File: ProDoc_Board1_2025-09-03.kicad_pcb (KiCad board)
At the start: 2 copper layers, 60 x 45.5 mm, 13 parts, among them CN10 A2502-WV02, CN11 A2502-WV02, CN2 B04B-XNISK-A-1(LF)(SN), CN3 B04B-XNISK-A-1(LF)(SN), CN4 B04B-XNISK-A-1(LF)(SN), CN7 XH2.54-5PIN, CN8 A2502-WV02, CN9 A2502-WV02, J1 Conn_01x05_Pin, U3 Ra-02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

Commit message: schenatic done
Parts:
- added C1: C_STAT, Capacitor_SMD:C_1210_3225Metric, B.Cu at (109.6, 53.1)
- added C2: C_PVL, Capacitor_SMD:C_0402_1005Metric, B.Cu at (98.5, 52.0)
- added C3: C_AVL, Capacitor_SMD:C_0402_1005Metric, B.Cu at (98.5, 50.0)
- added C4: C_BST2, Capacitor_SMD:C_0402_1005Metric, B.Cu at (98.5, 48.0)
- added C5: C_BST1, Capacitor_SMD:C_0402_1005Metric, B.Cu at (98.5, 46.1)
- added C6: C_BATT, Capacitor_SMD:C_0805_2012Metric, B.Cu at (103.0, 45.2)
- added C7: C_OUT1, Capacitor_SMD:C_1210_3225Metric_Pad1.33x2.70mm_HandSolder, B.Cu at (103.8, 53.1)
- added C8: C_OUT2, Capacitor_SMD:C_1210_3225Metric_Pad1.33x2.70mm_HandSolder, B.Cu at (103.8, 48.8)
- added C9: C_CHGIN, Capacitor_SMD:C_1210_3225Metric, B.Cu at (109.6, 48.8)
- added D1: LED, Diode_SMD:D_01005_0402Metric, B.Cu at (98.4, 44.3)
- added D3: D_Schottky_Small, Diode_SMD:D_SOD-323, B.Cu at (109.2, 60.0)
- added J2: Conn_01x02_Pin, Connector_JST:JST_SH_BM02B-SRSS-TB_1x02-1MP_P1.00mm_Vertical, B.Cu at (104.2, 64.6)
- added L1: L, ProDoc_Board1_2025-09-03:CMLE063T-2R2MS, B.Cu at (88.6, 52.2)
- added R1: R_OTGEN, Resistor_SMD:R_0805_2012Metric, B.Cu at (89.7, 66.2)
- added R10: R_ITO, Resistor_SMD:R_0805_2012Metric, B.Cu at (94.1, 54.4)
- added R11: R_VSET, Resistor_SMD:R_0805_2012Metric, B.Cu at (98.5, 66.2)
- added R12: R_INTB, Resistor_SMD:R_0805_2012Metric, B.Cu at (98.5, 63.3)
- added R13: R_SDA, Resistor_SMD:R_0805_2012Metric, B.Cu at (98.5, 60.3)
- added R14: R_SCL, Resistor_SMD:R_0805_2012Metric, B.Cu at (98.5, 57.4)
- added R15: R_SENSE, Resistor_SMD:R_1206_3216Metric, B.Cu at (109.6, 45.0)
- added R2: R_DISQBAT, Resistor_SMD:R_0805_2012Metric, B.Cu at (89.7, 63.3)
- added R3: R_STBY, Resistor_SMD:R_0805_2012Metric, B.Cu at (89.7, 60.3)
- added R4: R_TB, Resistor_SMD:R_0805_2012Metric, B.Cu at (89.7, 57.4)
- added R5: R_ISET, Resistor_SMD:R_0805_2012Metric, B.Cu at (89.7, 54.4)
- added R6: R_INOKB, Resistor_SMD:R_0805_2012Metric, B.Cu at (94.1, 66.2)
- added R7: R_STAT, Resistor_SMD:R_0805_2012Metric, B.Cu at (94.1, 63.3)
- added R8: R_PVL, Resistor_SMD:R_0805_2012Metric, B.Cu at (94.1, 60.3)
- added R9: R_INLIM, Resistor_SMD:R_0805_2012Metric, B.Cu at (94.1, 57.4)
- added U1: MAX77961EFV06+, ProDoc_Board1_2025-09-03:MAX77961, B.Cu at (142.6, 86.0)
- CN10: value A2502-WV02 -> BATT; moved to B.Cu
- CN11: value A2502-WV02 -> CHGIN; moved to B.Cu
- moved CN10 109.6 mm to (71.0, 59.7), turned to 0 degrees
- moved D2 85.3 mm to (78.3, 60.9), turned to 0 degrees
- moved CN11 50.3 mm to (127.5, 84.8), turned to -90 degrees
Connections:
- net Net-(U4-OUT+) renamed PULLUP
- CN10 pad 1: GND -> BATT-
- CN10 pad 2: Net-(CN10-Pad2) -> BATT+
- CN11 pad 1: Net-(CN10-Pad2) -> BATT-
- CN11 pad 2: Net-(D2-A) -> CSINN
- CN2 pad 1: GND -> BATT-
- CN3 pad 1: GND -> BATT-
- CN4 pad 1: GND -> BATT-
- CN7 pad 1: GND -> BATT-
- CN8 pad 1: GND -> BATT-
- CN9 pad 1: GND -> BATT-
- D2 pad 2: Net-(D2-A) -> SYS
- H1 pad 14: GND -> BATT-
- H1 pad 25: GND -> BATT-
- H1 pad 36: unconnected-(H1-Pad36) -> STAT
- H1 pad 39: GND -> BATT-
- H1 pad 9: GND -> BATT-
- J1 pad 4: GND -> BATT-
- J1 pad 5: GND -> BATT-
- U3 pad 16: GND -> BATT-
- U4 pad 2: GND -> BATT-
- U4 pad 4: GND -> BATT-
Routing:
- net Net-(D2-A): track 28.4 -> 0.00 mm, vias 2 -> 0
- net Net-(D2-K): track 25.7 -> 0.95 mm, vias 2 -> 0
- net Net-(CN10-Pad2): track 11.0 -> 0.00 mm
- net GND: vias 1 -> 0
- net BATT-: vias 0 -> 1
- added copper zone on B.Cu, net BATT-
- added copper zone on F.Cu, net BATT-
- removed copper zone on B.Cu, net GND
- removed copper zone on F.Cu, net GND

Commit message: layout started
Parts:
- added C10: C_CSINN, Capacitor_SMD:C_0402_1005Metric, B.Cu at (160.3, 82.6)
- added C11: C_CINP, Capacitor_SMD:C_0402_1005Metric, B.Cu at (161.7, 82.6)
- added C12: C_DIFF, Capacitor_SMD:C_0402_1005Metric, B.Cu at (161.0, 84.2)
- added R16: R_CSINP, Resistor_SMD:R_0402_1005Metric, B.Cu at (162.8, 82.6)
- added R17: R_CINN, Resistor_SMD:R_0402_1005Metric, B.Cu at (159.2, 82.5)
- C7, C8: footprint Capacitor_SMD:C_1210_3225Metric_Pad1.33x2.70mm_HandSolder -> Capacitor_SMD:C_1210_3225Metric
- CN10, CN11: footprint Connector_JST:JST_SH_BM02B-SRSS-TB_1x02-1MP_P1.00mm_Vertical -> Connector_JST:JST_VH_B2P-VH_1x02_P3.96mm_Vertical
- CN9: moved to B.Cu
- moved C7 67.0 mm to (159.0, 91.1), turned to 90 degrees
- moved C8 66.6 mm to (155.2, 91.1), turned to 90 degrees
- moved R15 62.3 mm to (161.0, 80.2), turned to 180 degrees
- moved C9 58.8 mm to (155.2, 86.0), turned to -90 degrees
- moved CN11 48.4 mm to (175.8, 84.2)
- moved CN9 6.23 mm to (126.6, 87.0), turned to 90 degrees
- moved U1 5.82 mm to (148.4, 86.6), turned to 90 degrees
- moved U4 2.47 mm to (156.0, 87.9)
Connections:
- C3 pad 1: Vavl -> PULLUP
- CN11 pad 2: CSINN -> Net-(CN11-Pad2)
- CN9 pad 2: PULLUP -> Net-(U4-OUT+)
- H1 pad 2: PULLUP -> Net-(U4-OUT+)
- R15 pad 1: CSINN -> Net-(CN11-Pad2)
- R4 pad 1: Vavl -> PULLUP
- R8 pad 2: Vavl -> PULLUP
- U1 pad 26: Vavl -> PULLUP
- U1 pad 29: CHGIN -> CSINP
- U4 pad 3: PULLUP -> Net-(U4-OUT+)
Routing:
- net PULLUP: track 13.3 -> 0.00 mm
- net Net-(D2-K): track 0.95 -> 0.00 mm

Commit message: temp
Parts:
- CN10, CN11: footprint Connector_JST:JST_VH_B2P-VH_1x02_P3.96mm_Vertical -> Connector_JST:JST_XH_B2B-XH-A_1x02_P2.50mm_Vertical
- R1, R10, R11, R12, R13, R14, R2, R3, R4, R5, R6, R7, R8, R9: footprint Resistor_SMD:R_0805_2012Metric -> Resistor_SMD:R_0402_1005Metric
- moved CN10 109.4 mm to (175.0, 93.7)
- moved L1 91.2 mm to (171.2, 90.9), turned to 90 degrees
- moved C4 68.3 mm to (151.6, 91.0), turned to 180 degrees
- moved C5 65.6 mm to (152.1, 83.9), turned to 180 degrees
- moved C6 64.6 mm to (148.0, 91.6), turned to 180 degrees
- moved R8 60.6 mm to (150.0, 83.8), turned to 180 degrees
- moved C2 59.7 mm to (150.7, 80.9), turned to 90 degrees
- moved C3 59.5 mm to (149.4, 80.9), turned to 90 degrees
- moved CN11 2.19 mm to (177.4, 85.7), turned to 180 degrees
- moved C7 2.01 mm to (158.8, 89.1)
- moved C8 2.01 mm to (155.0, 89.1)
- moved C9 1.81 mm to (155.0, 84.2)
- moved U1 1.66 mm to (149.9, 87.3)
- moved C10 0.58 mm to (160.0, 83.1)
- moved C11 0.58 mm to (161.4, 83.1)
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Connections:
- C1 pad 2: BATT- -> PGND
- C10 pad 2: BATT- -> PGND
- C11 pad 1: BATT- -> PGND
- C2 pad 2: BATT- -> PGND
- C3 pad 2: BATT- -> PGND
- C6 pad 2: BATT- -> PGND
- C7 pad 2: BATT- -> PGND
- C8 pad 2: BATT- -> PGND
- C9 pad 2: BATT- -> PGND
- CN11 pad 1: BATT- -> PGND
- CN2 pad 1: BATT- -> PGND
- CN3 pad 1: BATT- -> PGND
- CN4 pad 1: BATT- -> PGND
- CN7 pad 1: BATT- -> PGND
- CN8 pad 1: BATT- -> PGND
- CN9 pad 1: BATT- -> PGND
- H1 pad 14: BATT- -> PGND
- H1 pad 25: BATT- -> PGND
- H1 pad 39: BATT- -> PGND
- H1 pad 9: BATT- -> PGND
- J1 pad 4: BATT- -> PGND
- J1 pad 5: BATT- -> PGND
- R1 pad 1: BATT- -> PGND
- R10 pad 2: BATT- -> PGND
- R11 pad 2: BATT- -> PGND
- R2 pad 1: BATT- -> PGND
- R3 pad 2: BATT- -> PGND
- R5 pad 2: BATT- -> PGND
- R9 pad 2: BATT- -> PGND
- U1 pad 20: BATT- -> PGND
- U1 pad 4: BATT- -> PGND
- U3 pad 16: BATT- -> PGND
- U4 pad 2: BATT- -> PGND
- U4 pad 4: BATT- -> PGND

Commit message: layout started
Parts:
- added C13: C_SYSA, Capacitor_SMD:C_0402_1005Metric, B.Cu at (145.2, 87.3)
- CN9: moved to F.Cu
- moved D2 90.6 mm to (162.6, 94.2), turned to 180 degrees
- moved R2 68.0 mm to (150.8, 93.2), turned to 90 degrees
- moved R1 67.8 mm to (151.9, 93.2), turned to 90 degrees
- moved R3 65.5 mm to (151.7, 81.5), turned to 90 degrees
- moved R4 63.9 mm to (144.2, 90.8)
- moved R5 61.7 mm to (143.5, 84.7), turned to 180 degrees
- moved R10 60.8 mm to (148.5, 81.5), turned to 90 degrees
- moved R9 57.0 mm to (143.5, 85.8), turned to 180 degrees
- moved D1 55.7 mm to (135.4, 86.0), turned to 180 degrees
- moved R14 55.3 mm to (143.5, 89.6)
- moved R13 53.1 mm to (143.5, 88.4)
- moved R11 51.1 mm to (147.3, 81.5), turned to 90 degrees
- moved R12 50.8 mm to (143.5, 86.9), turned to 180 degrees
- moved R6 48.4 mm to (138.3, 85.9), turned to 180 degrees
- moved R7 47.7 mm to (134.5, 88.7), turned to 180 degrees
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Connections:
- net Net-(CN11-Pad2) renamed /VBUS
- net Net-(U1-LX1) renamed /LX1
- net Net-(U1-LX2) renamed /LX2
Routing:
- net PGND: track 0.00 -> 20.5 mm, vias 0 -> 13
- net /LX1: track 0.00 -> 8.24 mm, vias 0 -> 2
- net /LX2: track 0.00 -> 4.94 mm
- net CHGIN: track 0.00 -> 4.41 mm
- net Net-(J1-Pin_3): track 22.9 -> 20.5 mm
- added copper zone on B.Cu, net (none)
- added copper zone on B.Cu, net /LX1
- added copper zone on B.Cu, net /LX2
- added copper zone on B.Cu, net /VBUS
- added copper zone on B.Cu, net CHGIN
- added copper zone on B.Cu, net CSINN
- added copper zone on B.Cu, net CSINP
- added copper zone on B.Cu, net PGND
- added copper zone on F.Cu, net PGND
- removed copper zone on B.Cu, net BATT-
- removed copper zone on F.Cu, net BATT-

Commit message: v1.2.0
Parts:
- removed D1: LED, Diode_SMD:D_01005_0402Metric
- CN2, CN3, CN4, CN7, CN8, J1: moved to B.Cu
- J2: moved to F.Cu
- moved J1 51.1 mm to (178.4, 108.8), turned to -90 degrees
- moved CN7 38.8 mm to (132.2, 106.7), turned to 0 degrees
- moved CN8 35.8 mm to (133.8, 112.5), turned to 180 degrees
- moved CN3 31.5 mm to (168.7, 111.2), turned to 0 degrees
- moved CN2 31.5 mm to (168.7, 105.5), turned to 0 degrees
- moved CN4 31.4 mm to (168.7, 116.9), turned to 0 degrees
- moved C13 1.80 mm to (145.3, 85.5)
- moved CN9 1.00 mm to (125.6, 86.9)
- moved R10 1.00 mm to (147.5, 81.5)
- moved R11 1.00 mm to (146.3, 81.5)
- moved C4 0.60 mm to (151.0, 91.2)
- moved R12 0.51 mm to (143.0, 86.8)
- moved U4 0.31 mm to (156.3, 87.9)
- turned J2 to 180 degrees
- turned H1 to 180 degrees
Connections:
- CN2 pad 2: Net-(CN2-Pad2) -> SCL
- CN2 pad 3: Net-(CN2-Pad3) -> SDA
- CN3 pad 2: Net-(CN2-Pad2) -> SCL
- CN3 pad 3: Net-(CN2-Pad3) -> SDA
- CN4 pad 2: Net-(CN2-Pad2) -> SCL
- CN4 pad 3: Net-(CN2-Pad3) -> SDA
- H1 pad 3: Net-(CN2-Pad3) -> SDA
- H1 pad 38: unconnected-(H1-Pad38) -> INOKB
- H1 pad 40: unconnected-(H1-Pad40) -> INTB
- H1 pad 5: Net-(CN2-Pad2) -> SCL
- R12 pad 1: Net-(U1-INTB) -> INTB
- R13 pad 2: Net-(U1-SDA) -> SDA
- R14 pad 2: Net-(U1-SCL) -> SCL
- R6 pad 1: Net-(U1-INOKB) -> INOKB
- R6 pad 2: Net-(D1-K) -> PULLUP
- U1 pad 14: Net-(U1-SCL) -> SCL
- U1 pad 15: Net-(U1-SDA) -> SDA
- U1 pad 17: Net-(U1-INOKB) -> INOKB
- U1 pad 18: Net-(U1-INTB) -> INTB
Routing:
- net Net-(U4-OUT+): track 0.11 -> 90.2 mm
- net BATT-: track 0.00 -> 80.8 mm
- net SDA: track 0.00 -> 72.2 mm, vias 0 -> 2
- net SCL: track 0.00 -> 53.8 mm, vias 0 -> 1
- net BATT+: track 0.00 -> 47.2 mm
- net PULLUP: track 0.00 -> 39.2 mm, vias 0 -> 6
- net PGND: track 20.5 -> 55.2 mm, vias 13 -> 30
- net /LX2: track 4.94 -> 37.9 mm, vias 0 -> 2
- net SYS: track 0.00 -> 32.3 mm, vias 0 -> 2
- net INOKB: track 0.00 -> 29.4 mm, vias 0 -> 1
- net INTB: track 0.00 -> 28.8 mm, vias 0 -> 1
- net Net-(J2-Pin_2): track 0.00 -> 24.9 mm, vias 0 -> 1
- net Net-(CN2-Pad3): track 19.9 -> 0.00 mm
- net Net-(CN2-Pad2): track 17.9 -> 0.00 mm
- net CSINP: track 0.00 -> 17.5 mm, vias 0 -> 2
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- added copper zone on B.Cu, net BATT+
- added copper zone on B.Cu, net SYS
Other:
- board text added: "1"
- board text added: "2"

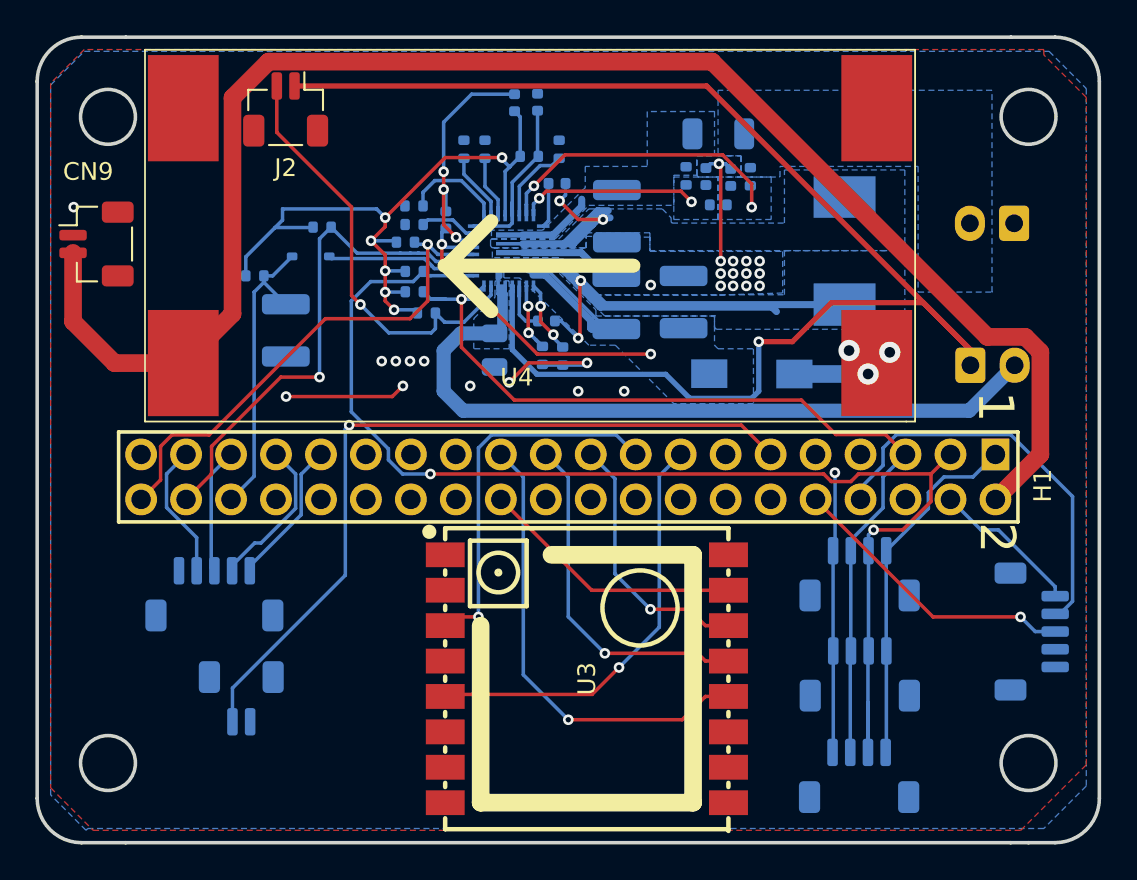
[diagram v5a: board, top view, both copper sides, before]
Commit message: fixed grounds
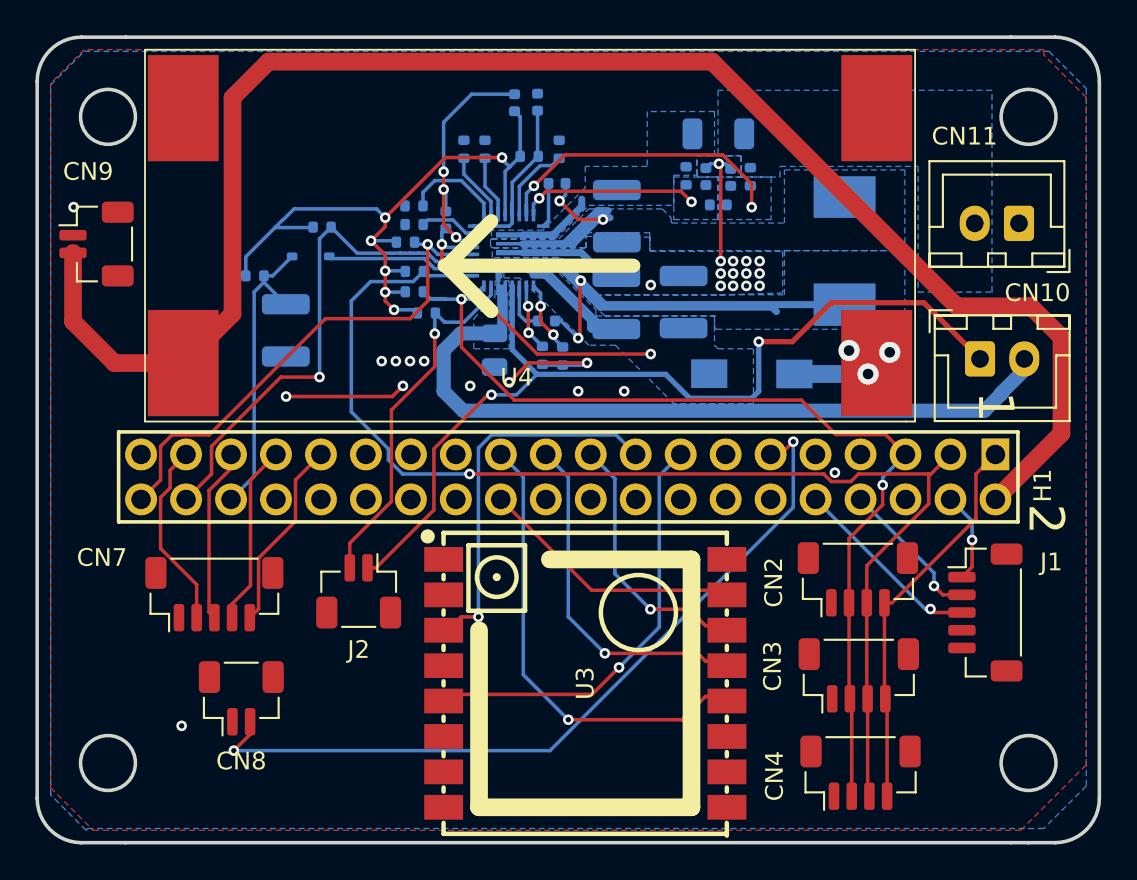
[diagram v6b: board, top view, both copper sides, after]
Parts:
- CN10, CN11, CN2, CN3, CN4, CN7, CN8, J1: moved to F.Cu
- moved J2 27.5 mm to (140.4, 106.5)
- moved J1 2.83 mm to (175.8, 107.7)
- moved CN10 0.65 mm to (175.5, 93.4)
- moved CN2 0.31 mm to (168.6, 105.8)
- moved U3 0.28 mm to (153.2, 111.7)
- moved CN11 0.27 mm to (177.7, 85.7)
- moved CN4 0.19 mm to (168.7, 116.8)
- moved CN3 0.08 mm to (168.6, 111.3)
- turned CN8 to 0 degrees
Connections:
- C1 pad 2: PGND -> BATT-
- C10 pad 2: PGND -> BATT-
- C11 pad 1: PGND -> BATT-
- C13 pad 2: PGND -> BATT-
- C2 pad 2: PGND -> BATT-
- C3 pad 2: PGND -> BATT-
- C6 pad 2: PGND -> BATT-
- C7 pad 2: PGND -> BATT-
- C8 pad 2: PGND -> BATT-
- C9 pad 2: PGND -> BATT-
- CN11 pad 1: PGND -> BATT-
- CN2 pad 1: PGND -> BATT-
- CN3 pad 1: PGND -> BATT-
- CN4 pad 1: PGND -> BATT-
- CN7 pad 1: PGND -> BATT-
- CN8 pad 1: PGND -> BATT-
- CN9 pad 1: PGND -> BATT-
- H1 pad 14: PGND -> BATT-
- H1 pad 25: PGND -> BATT-
- H1 pad 39: PGND -> BATT-
- H1 pad 9: PGND -> BATT-
- J1 pad 4: PGND -> BATT-
- J1 pad 5: PGND -> BATT-
- R1 pad 1: PGND -> BATT-
- R10 pad 2: PGND -> BATT-
- R11 pad 2: PGND -> BATT-
- R2 pad 1: PGND -> BATT-
- R3 pad 2: PGND -> BATT-
- R5 pad 2: PGND -> BATT-
- R9 pad 2: PGND -> BATT-
- U1 pad 20: PGND -> BATT-
- U1 pad 4: PGND -> BATT-
- U3 pad 16: PGND -> BATT-
- U4 pad 2: PGND -> BATT-
- U4 pad 4: PGND -> BATT-
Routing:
- net PGND: track 55.2 -> 0.00 mm, vias 30 -> 0
- net Net-(J1-Pin_2): track 23.1 -> 9.04 mm, vias 0 -> 1
- net BATT-: track 80.8 -> 91.8 mm, vias 1 -> 33
- net Net-(J1-Pin_3): track 16.6 -> 10.9 mm
- net Net-(J2-Pin_2): track 24.9 -> 21.1 mm
- net Net-(J1-Pin_1): track 8.49 -> 5.13 mm, vias 0 -> 1
- net Net-(CN7-Pad2): track 7.73 -> 10.7 mm
- net Net-(CN7-Pad3): track 7.11 -> 9.86 mm
- net Net-(CN7-Pad5): track 8.24 -> 10.9 mm
- net Net-(U4-OUT+): track 90.2 -> 92.4 mm
- net SCL: track 53.8 -> 55.7 mm, vias 1 -> 2
- net Net-(CN2-Pad4): track 20.4 -> 22.2 mm
- net Net-(CN7-Pad4): track 8.73 -> 10.2 mm
- net SDA: track 72.2 -> 70.7 mm, vias 2 -> 1
- net BATT+: track 47.2 -> 48.3 mm
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- added copper zone on B.Cu, net BATT-
- added copper zone on F.Cu, net BATT-
- removed copper zone on B.Cu, net PGND
- removed copper zone on F.Cu, net PGND
